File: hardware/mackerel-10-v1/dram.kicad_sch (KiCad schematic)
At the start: 30 parts, among them J2 Conn_02x05_Odd_Even

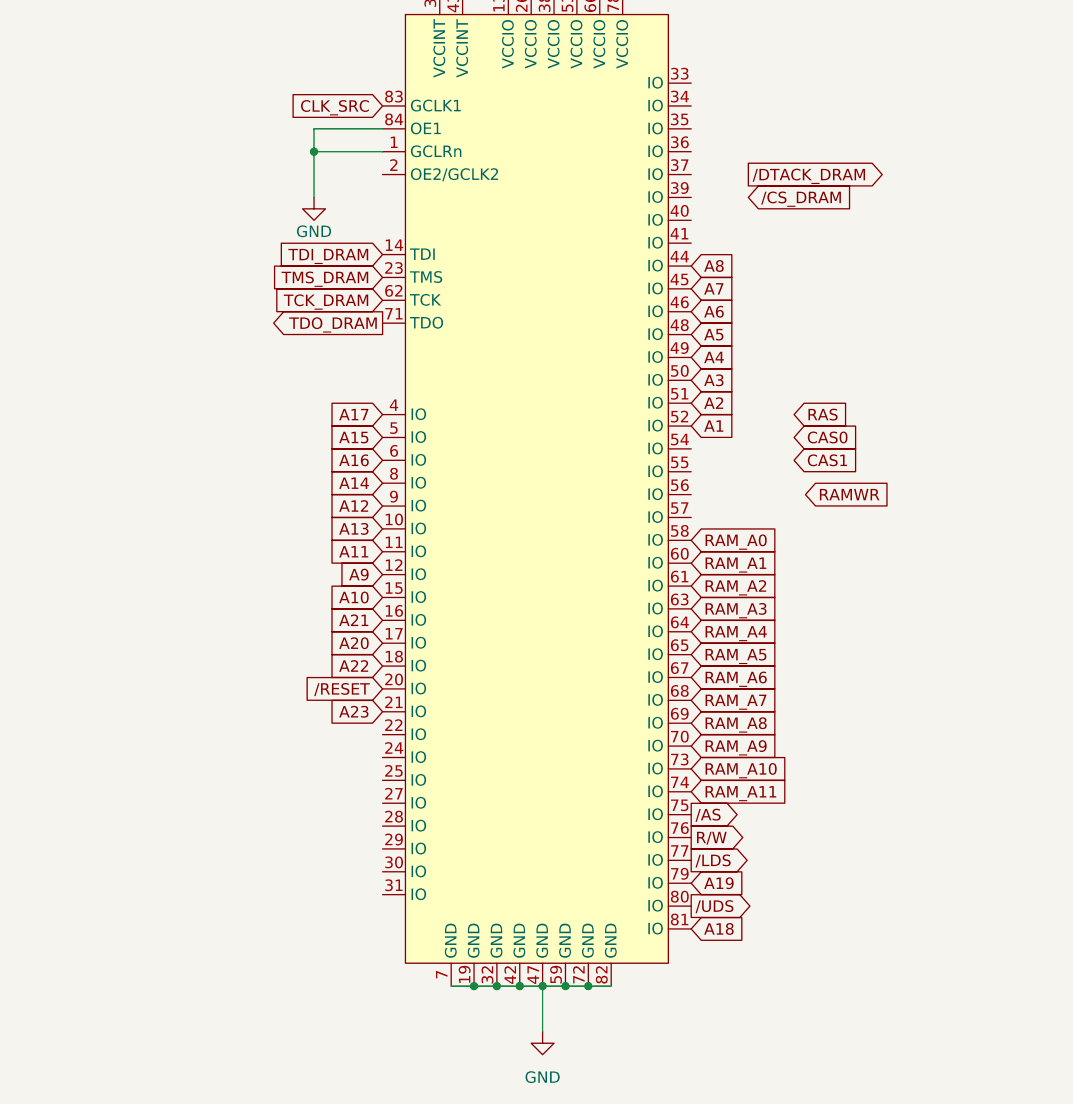
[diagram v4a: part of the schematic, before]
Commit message: DRAM controller mostly routed
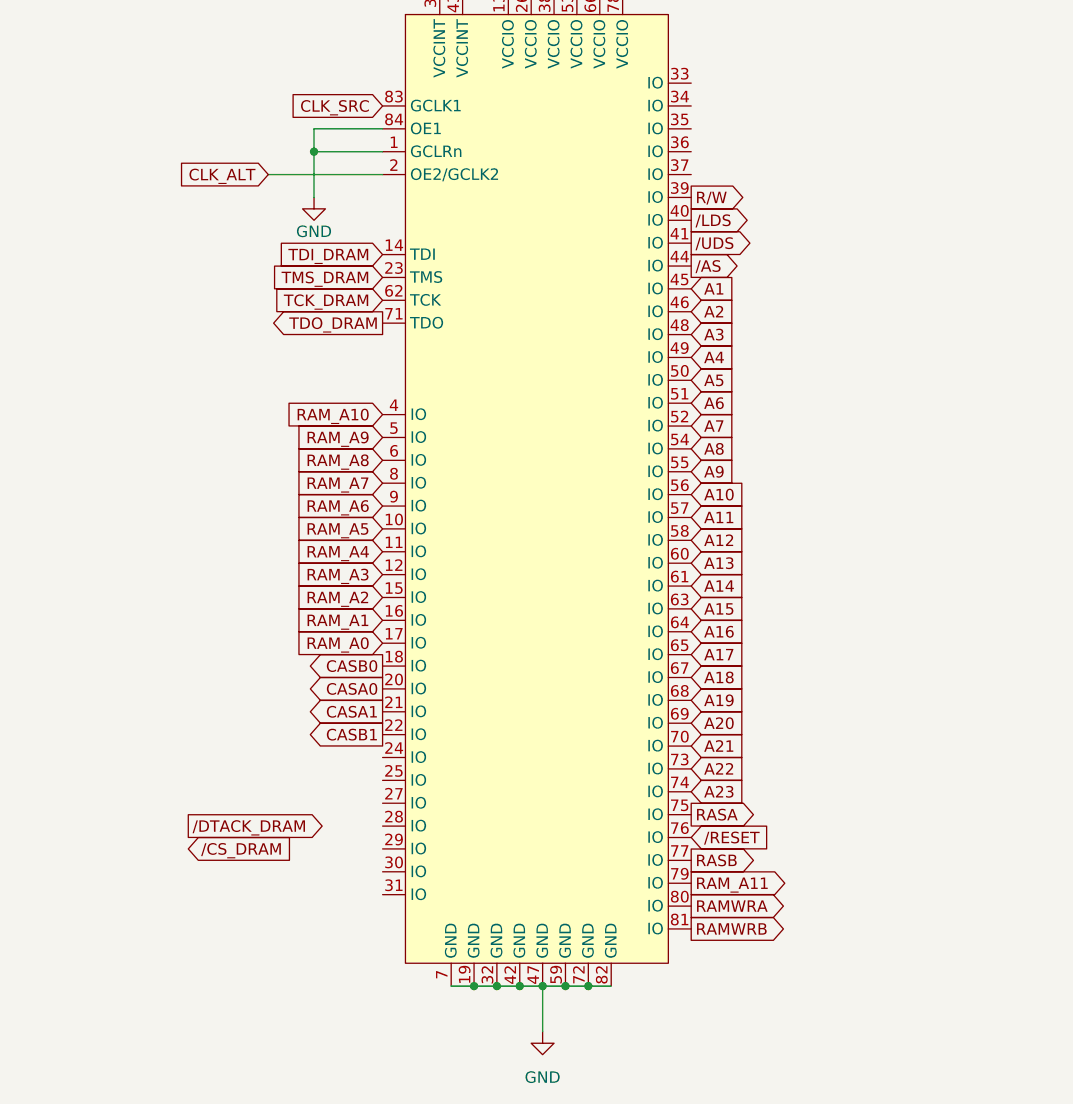
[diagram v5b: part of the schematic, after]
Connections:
- net A1: now also U11.45 (IO); no longer U11.52 (IO)
- net A10: now also U11.56 (IO); no longer U11.15 (IO)
- net A11: now also U11.57 (IO); no longer U11.11 (IO)
- net A12: now also U11.58 (IO); no longer U11.9 (IO)
- net A13: now also U11.60 (IO); no longer U11.10 (IO)
- net A14: now also U11.61 (IO); no longer U11.8 (IO)
- net A15: now also U11.63 (IO); no longer U11.5 (IO)
- net A16: now also U11.64 (IO); no longer U11.6 (IO)
- net A17: now also U11.65 (IO); no longer U11.4 (IO)
- net A18: now also U11.67 (IO); no longer U11.81 (IO)
- net A19: now also U11.68 (IO); no longer U11.79 (IO)
- net A2: now also U11.46 (IO); no longer U11.51 (IO)
- net A20: now also U11.69 (IO); no longer U11.17 (IO)
- net A21: now also U11.70 (IO); no longer U11.16 (IO)
- net A22: now also U11.73 (IO); no longer U11.18 (IO)
- net A23: now also U11.74 (IO); no longer U11.21 (IO)
- net A3: now also U11.48 (IO); no longer U11.50 (IO)
- net A5: now also U11.50 (IO); no longer U11.48 (IO)
- net A6: now also U11.51 (IO); no longer U11.46 (IO)
- net A7: now also U11.52 (IO); no longer U11.45 (IO)
- net A8: now also U11.54 (IO); no longer U11.44 (IO)
- net A9: now also U11.55 (IO); no longer U11.12 (IO)
- net CASA0: now also U11.20 (IO)
- net CASA1: now also U11.21 (IO)
- net CASB0: now also U11.18 (IO)
- net CASB1: now also U11.22 (IO)
- net RAMWRA: now also U11.80 (IO)
- net RAMWRB: now also U11.81 (IO)
- net RAM_A0: now also U11.17 (IO); no longer U11.58 (IO)
- net RAM_A1: now also U11.16 (IO); no longer U11.60 (IO)
- net RAM_A10: now also U11.4 (IO); no longer U11.73 (IO)
- net RAM_A11: now also U11.79 (IO); no longer U11.74 (IO)
- net RAM_A2: now also U11.15 (IO); no longer U11.61 (IO)
- net RAM_A3: now also U11.12 (IO); no longer U11.63 (IO)
- net RAM_A4: now also U11.11 (IO); no longer U11.64 (IO)
- net RAM_A5: now also U11.10 (IO); no longer U11.65 (IO)
- net RAM_A6: now also U11.9 (IO); no longer U11.67 (IO)
- net RAM_A7: now also U11.8 (IO); no longer U11.68 (IO)
- net RAM_A8: now also U11.6 (IO); no longer U11.69 (IO)
- net RAM_A9: now also U11.5 (IO); no longer U11.70 (IO)
- net RASA: now also U11.75 (IO)
- net RASB: now also U11.77 (IO)
- net R/W: now also U11.39 (IO); no longer U11.76 (IO)
- net /AS: now also U11.44 (IO); no longer U11.75 (IO)
- net /LDS: now also U11.40 (IO); no longer U11.77 (IO)
- net /RESET: now also U11.76 (IO); no longer U11.20 (IO)
- net /UDS: now also U11.41 (IO); no longer U11.80 (IO)
- net CLK_ALT: now reaches U11.2 (OE2/GCLK2)

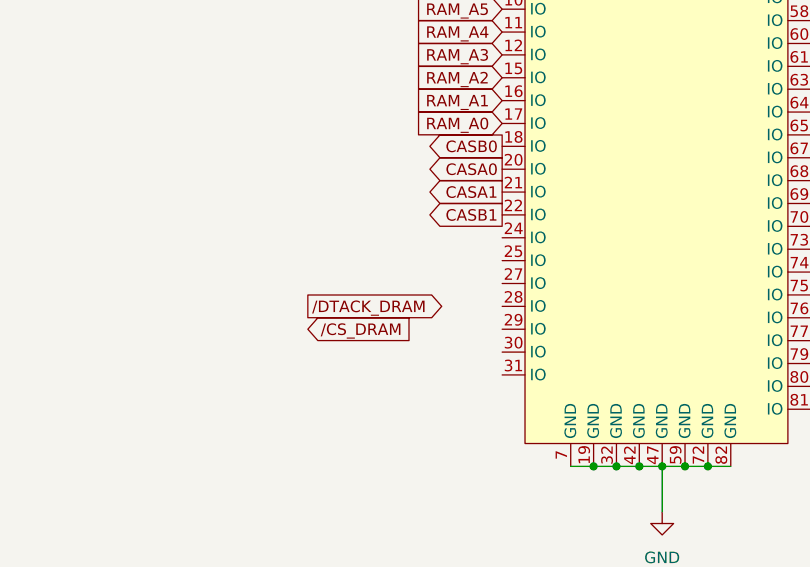
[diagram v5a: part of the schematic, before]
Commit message: Glue logic CPLD almost fully routed
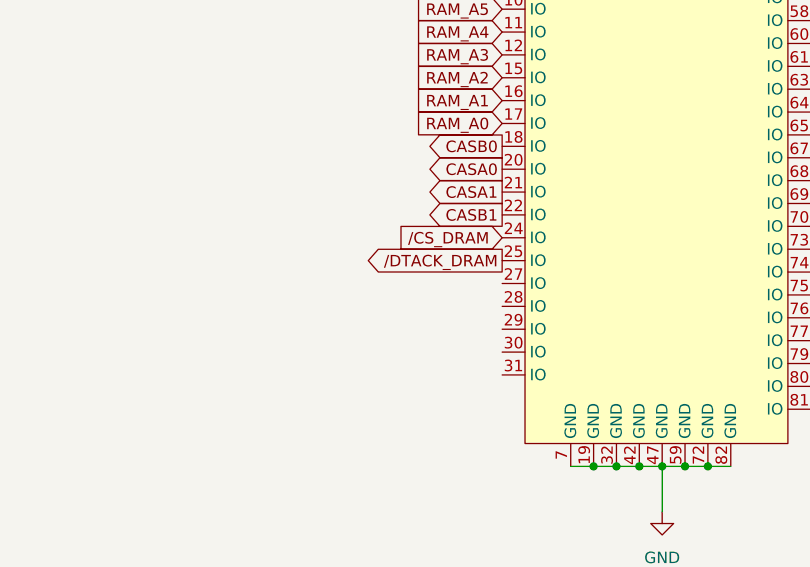
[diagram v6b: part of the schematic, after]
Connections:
- net /CS_DRAM: now also U11.24 (IO)
- net /DTACK_DRAM: now also U11.25 (IO)
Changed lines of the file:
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@@
+		)
+	)
+	(global_label "{slash}CS_DRAM"
+		(shape input)
+		(at 201.93 119.38 180)
+		(fields_autoplaced yes)
+		(effects
+			(font
+				(size 1.27 1.27)
+			)
+			(justify right)
+		)
+		(property "Intersheetrefs" "${INTERSHEET_REFS}"
+			(at 189.0872 119.38 0)
+			(effects
+				(font
+					(size 1.27 1.27)
+				)
+				(justify right)
+				(hide yes)
+			)
 		)
 	)
@@
 		)
 	)
-	(global_label "{slash}CS_DRAM"
-		(shape input)
-		(at 180.34 129.54 0)
-		(fields_autoplaced yes)
-		(effects
-			(font
-				(size 1.27 1.27)
-			)
-			(justify left)
-		)
-		(property "Intersheetrefs" "${INTERSHEET_REFS}"
-			(at 193.1828 129.54 0)
-			(effects
-				(font
-					(size 1.27 1.27)
-				)
-				(justify left)
-				(hide yes)
-			)
-		)
-	)
 	(global_label "TMS_DRAM"
 		(shape output)
@@
 		)
 	)
-	(global_label "{slash}DTACK_DRAM"
-		(shape output)
-		(at 180.34 127 0)
-		(fields_autoplaced yes)
-		(effects
-			(font
-				(size 1.27 1.27)
-			)
-			(justify left)
-		)
-		(property "Intersheetrefs" "${INTERSHEET_REFS}"
-			(at 196.5695 127 0)
-			(effects
-				(font
-					(size 1.27 1.27)
-				)
-				(justify left)
-				(hide yes)
-			)
-		)
-	)
 	(global_label "D2"
 		(shape bidirectional)
@@
 			(effects
 				(font
+					(size 1.27 1.27)
+				)
+				(justify right)
+				(hide yes)
+			)
+		)
+	)
+	(global_label "{slash}DTACK_DRAM"
+		(shape output)
+		(at 201.93 121.92 180)
+		(fields_autoplaced yes)
+		(effects
+			(font
+				(size 1.27 1.27)
+			)
+			(justify right)
+		)
+		(property "Intersheetrefs" "${INTERSHEET_REFS}"
+			(at 185.7005 121.92 0)
+			(effects
+				(font

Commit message: Mack-10 v1 fully routed
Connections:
- no-connect marks 15 -> 25
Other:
- note removed: "TODO: add two more RAM sticks?"
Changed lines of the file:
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@@
+	)
+	(no_connect
+		(at 201.93 132.08)
+	)
+	(no_connect
+		(at 236.22 52.07)
 	)
 	(no_connect
@@
 	)
 	(no_connect
+		(at 236.22 49.53)
+	)
+	(no_connect
+		(at 236.22 44.45)
+	)
+	(no_connect
 		(at 58.42 124.46)
 	)
@@
 	)
 	(no_connect
+		(at 201.93 124.46)
+	)
+	(no_connect
+		(at 201.93 129.54)
+	)
+	(no_connect
+		(at 201.93 134.62)
+	)
+	(no_connect
 		(at 120.65 46.99)
 	)
 	(no_connect
+		(at 236.22 46.99)
+	)
+	(no_connect
 		(at 125.73 168.91)
 	)
@@
 	)
 	(no_connect
+		(at 236.22 54.61)
+	)
+	(no_connect
 		(at 113.03 171.45)
 	)
@@
 	(no_connect
 		(at 120.65 49.53)
+	)
+	(no_connect
+		(at 201.93 127)
 	)
 	(no_connect
@@
 	(text "TODO: add some test points!"
 		(exclude_from_sim no)
-		(at 108.204 -28.194 0)
+		(at 150.876 78.232 0)
 		(effects
 			(font
-				(size 1.27 1.27)
-			)
-		)
-	)
-	(text "TODO: add two more RAM sticks?"
-		(exclude_from_sim no)
-		(at 99.568 -11.938 0)
-		(effects
-			(font

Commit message: Mackerel-10 v1 release
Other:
- note removed: "TODO: add some test points!"
- moved on the sheet: C1, C10, C11, C12, C13, C14, C15, C2, C3, C33, C34, C35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
